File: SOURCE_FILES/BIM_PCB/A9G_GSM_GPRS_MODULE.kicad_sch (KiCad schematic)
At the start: 46 parts, among them J3 nano_sim, Q5 BSN20, U3 A9G_MODULE

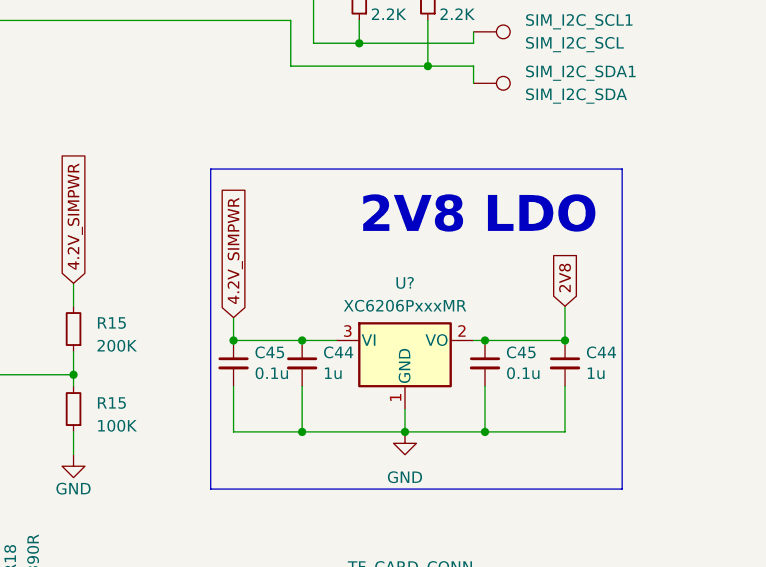
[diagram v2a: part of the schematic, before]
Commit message: completed gerber and placement
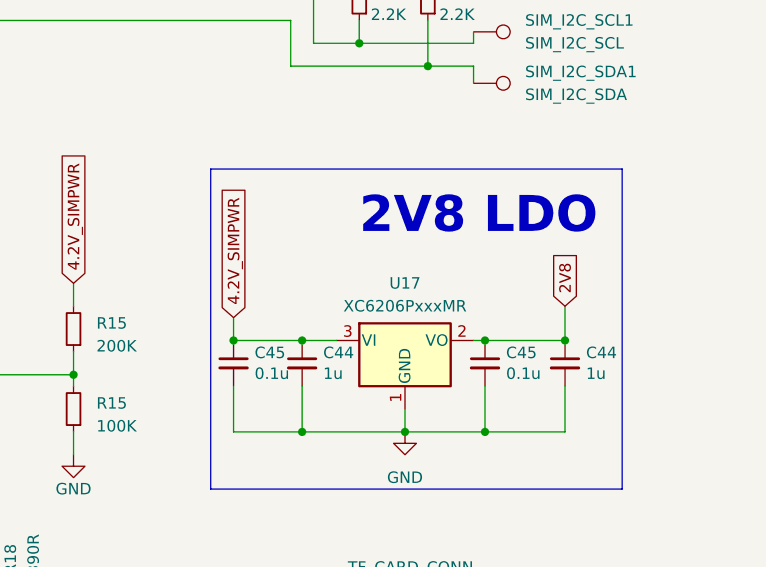
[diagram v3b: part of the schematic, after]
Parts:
- gave numbers to parts that had none: 1
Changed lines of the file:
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@@
           (reference "C15") (unit 1)
-        )
-        (path "/b79ebed7-e146-448b-8dab-0aefb3e182ca/2c1557a8-70b5-4535-b084-9e551cb55dcd/4ded7b71-30ec-4263-8ef5-be9822f9dd9f"
-          (reference "C?") (unit 1)
         )
       )
@@
           (reference "#PWR0125") (unit 1)
         )
-        (path "/b79ebed7-e146-448b-8dab-0aefb3e182ca/2c1557a8-70b5-4535-b084-9e551cb55dcd/4ded7b71-30ec-4263-8ef5-be9822f9dd9f"
-          (reference "#PWR0125") (unit 1)
-        )
       )
     )
@@
   (symbol (lib_id "Regulator_Linear:XC6206PxxxMR") (at 259.08 106.68 0) (unit 1)
     (in_bom yes) (on_board yes) (dnp no) (fields_autoplaced)
-    (property "Reference" "U?" (at 259.08 100.33 0)
+    (property "Reference" "U17" (at 259.08 100.33 0)
       (effects (font (size 1.27 1.27)))
     )
@@
     (instances
       (project "BIM_PCB"
-        (path "/b79ebed7-e146-448b-8dab-0aefb3e182ca/2c1557a8-70b5-4535-b084-9e551cb55dcd/4ded7b71-30ec-4263-8ef5-be9822f9dd9f"
-          (reference "U?") (unit 1)
-        )
         (path "/b79ebed7-e146-448b-8dab-0aefb3e182ca/2c1557a8-70b5-4535-b084-9e551cb55dcd"
           (reference "U17") (unit 1)
@@
           (reference "C16") (unit 1)
         )
-        (path "/b79ebed7-e146-448b-8dab-0aefb3e182ca/2c1557a8-70b5-4535-b084-9e551cb55dcd/4ded7b71-30ec-4263-8ef5-be9822f9dd9f"
-          (reference "C?") (unit 1)
-        )
       )
       (project "sd_card"
@@
           (reference "C14") (unit 1)
         )
-        (path "/b79ebed7-e146-448b-8dab-0aefb3e182ca/2c1557a8-70b5-4535-b084-9e551cb55dcd/4ded7b71-30ec-4263-8ef5-be9822f9dd9f"
-          (reference "C?") (unit 1)
-        )
       )
       (project "sd_card"
@@
           (reference "C17") (unit 1)
         )
-        (path "/b79ebed7-e146-448b-8dab-0aefb3e182ca/2c1557a8-70b5-4535-b084-9e551cb55dcd/4ded7b71-30ec-4263-8ef5-be9822f9dd9f"
-          (reference "C?") (unit 1)
-        )
-      )
+      )

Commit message: updates in BOM gerber and PCL
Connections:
- net GND: now also U3.29 (GND), U3.46 (GND); no longer U3.40 (GND)
- net GPS POSITION: now also U3.30 (IO28); no longer U3.39 (IO28)
- net Sim_CLK: now also U3.41 (SIM_CLK); no longer U3.28 (SIM_CLK)
- net Sim_DIO: now also U3.39 (SIM_DIO); no longer U3.30 (SIM_DIO)
- net V_Sim: now also U3.40 (VSIM); no longer U3.29 (VSIM)
- net at U3.31 (IO30): no longer D+1.1
- net at U3.32 (IO25): no longer D-1.1
- net at U3.33 (MIC_N): no longer D+1.1
- net at U3.34 (MIC_P): no longer D-1.1
- net at U3.35 (USB_N): now also D-1.1
- net at U3.36 (USB_P): now also D+1.1
- net at U3.37 (HST_TXD): now also D+1.1
- net at U3.38 (HST_RXD): now also D-1.1
- net at AE2.1 (A), D1.2 (A2), L2.2: now also U3.28 (GPS_RF); no longer U3.41 (GPS_RF)
- net i/o: now reaches D11.5 (K), J3.C7 (I/O), R15.2
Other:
- moved on the sheet: D+1, D-1, D13, R18
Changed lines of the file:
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@@
   (junction (at 108.585 91.44) (diameter 0) (color 0 0 0 0)
   )
-  (junction (at 157.48 170.18) (diameter 0) (color 0 0 0 0)
-  )
   (junction (at 73.025 91.44) (diameter 0) (color 0 0 0 0)
   )
@@
   (junction (at 247.65 106.68) (diameter 0) (color 0 0 0 0)
   )
+  (junction (at 165.1 170.18) (diameter 0) (color 0 0 0 0)
+  )
   (junction (at 267.97 106.68) (diameter 0) (color 0 0 0 0)
   )
@@
   (junction (at 62.865 29.21) (diameter 0) (color 0 0 0 0)
   )
+  (junction (at 170.18 170.18) (diameter 0) (color 0 0 0 0)
+  )
   (junction (at 247.65 116.84) (diameter 0) (color 0 0 0 0)
   )
   (no_connect (at 187.96 114.3))
   (no_connect (at 66.04 99.06))
-  (no_connect (at 134.62 152.4))
+  (no_connect (at 134.62 154.94))
   (no_connect (at 134.62 121.92))
   (no_connect (at 187.96 109.22))
@@
   (no_connect (at 187.96 111.76))
   (no_connect (at 187.96 91.44))
-  (no_connect (at 134.62 149.86))
+  (no_connect (at 134.62 152.4))
   (no_connect (at 134.62 134.62))
   (no_connect (at 187.96 93.98))
@@
     (stroke (width 0) (type default))
   )
+  (wire (pts (xy 165.1 165.1) (xy 165.1 170.18))
+    (stroke (width 0) (type default))
+  )
   (wire (pts (xy 187.96 142.24) (xy 252.73 142.24))
     (stroke (width 0) (type default))
@@
     (stroke (width 0) (type default))
   )
-  (wire (pts (xy 157.48 165.1) (xy 157.48 170.18))
-    (stroke (width 0) (type default))
-  )
-  (wire (pts (xy 157.48 170.18) (xy 162.56 170.18))
-    (stroke (width 0) (type default))
-  )
   (wire (pts (xy 240.03 116.84) (xy 247.65 116.84))
     (stroke (width 0) (type default))
@@
     (stroke (width 0) (type default))
   )
-  (wire (pts (xy 134.62 142.24) (xy 129.54 142.24))
+  (wire (pts (xy 134.62 144.78) (xy 128.905 144.78))
     (stroke (width 0) (type default))
   )
@@
     (stroke (width 0) (type default))
   )
+  (wire (pts (xy 170.18 165.1) (xy 170.18 170.18))
+    (stroke (width 0) (type default))
+  )
   (wire (pts (xy 109.22 40.64) (xy 134.62 40.64))
     (stroke (width 0) (type default))
@@
     (stroke (width 0) (type default))
   )
-  (wire (pts (xy 116.84 163.83) (xy 116.84 167.005))
+  (wire (pts (xy 116.84 166.37) (xy 116.84 169.545))
     (stroke (width 0) (type default))
   )
@@
     (stroke (width 0) (type default))
   )
+  (wire (pts (xy 170.18 170.18) (xy 172.72 170.18))
+    (stroke (width 0) (type default))
+  )
   (wire (pts (xy 100.33 93.98) (xy 134.62 93.98))
     (stroke (width 0) (type default))
@@
     (stroke (width 0) (type default))
   )
-  (wire (pts (xy 129.54 142.24) (xy 129.54 146.05))
+  (wire (pts (xy 128.905 144.78) (xy 128.905 148.59))
     (stroke (width 0) (type default))
   )
@@
     (stroke (width 0) (type default))
   )
-  (wire (pts (xy 116.84 154.94) (xy 134.62 154.94))
+  (wire (pts (xy 116.84 157.48) (xy 134.62 157.48))
     (stroke (width 0) (type default))
   )
@@
     (stroke (width 0) (type default))
   )
-  (wire (pts (xy 116.84 151.13) (xy 132.08 151.13))
+  (wire (pts (xy 116.84 153.67) (xy 132.08 153.67))
     (stroke (width 0) (type default))
   )
@@
     (stroke (width 0) (type default))
   )
-  (wire (pts (xy 152.4 170.18) (xy 157.48 170.18))
+  (wire (pts (xy 152.4 170.18) (xy 162.56 170.18))
     (stroke (width 0) (type default))
   )
@@
     (stroke (width 0) (type default))
   )
-  (wire (pts (xy 132.08 144.78) (xy 134.62 144.78))
+  (wire (pts (xy 132.08 147.32) (xy 134.62 147.32))
     (stroke (width 0) (type default))
   )
@@
     (stroke (width 0) (type default))
   )
-  (wire (pts (xy 129.54 146.05) (xy 116.84 146.05))
+  (wire (pts (xy 128.905 148.59) (xy 116.84 148.59))
     (stroke (width 0) (type default))
   )
@@
     (stroke (width 0) (type default))
   )
-  (wire (pts (xy 116.84 172.085) (xy 116.84 176.53))
+  (wire (pts (xy 116.84 174.625) (xy 116.84 179.07))
     (stroke (width 0) (type default))
   )
@@
     (stroke (width 0) (type default))
   )
+  (wire (pts (xy 165.1 170.18) (xy 170.18 170.18))
+    (stroke (width 0) (type default))
+  )
   (wire (pts (xy 269.24 24.765) (xy 269.24 24.13))
     (stroke (width 0) (type default))
@@
     (stroke (width 0) (type default))
   )
-  (wire (pts (xy 116.84 154.94) (xy 116.84 158.75))
+  (wire (pts (xy 116.84 157.48) (xy 116.84 161.29))
     (stroke (width 0) (type default))
   )
@@
     (stroke (width 0) (type default))
   )
-  (wire (pts (xy 162.56 170.18) (xy 172.72 170.18))
+  (wire (pts (xy 162.56 170.18) (xy 165.1 170.18))
     (stroke (width 0) (type default))
   )
-  (wire (pts (xy 132.08 151.13) (xy 132.08 144.78))
+  (wire (pts (xy 132.08 153.67) (xy 132.08 147.32))
     (stroke (width 0) (type default))
   )
@@
     (effects (font (size 1 1) bold) (justify right bottom))
   )
+  (label "i{slash}o" (at 69.85 101.6 0) (fields_autoplaced)
+    (effects (font (size 1.27 1.27)) (justify left bottom))
+  )
   (label "IO29" (at 97.79 59.69 0) (fields_autoplaced)
     (effects (font (size 1.27 1.27) bold) (justify left bottom))
@@
     (effects (font (size 1.27 1.27)) (justify right bottom))
   )
-  (label "GPS POSITION" (at 118.11 154.94 0) (fields_autoplaced)
+  (label "GPS POSITION" (at 118.11 157.48 0) (fields_autoplaced)
     (effects (font (size 1.27 1.27)) (justify left bottom))
   )
@@
     )
   )
-  (symbol (lib_id "Device:R_Small") (at 116.84 161.29 0) (mirror y) (unit 1)
+  (symbol (lib_id "Device:R_Small") (at 116.84 163.83 0) (mirror y) (unit 1)
     (in_bom yes) (on_board yes) (dnp no) (fields_autoplaced)
-    (property "Reference" "R18" (at 118.745 160.655 0)
+    (property "Reference" "R18" (at 118.745 163.195 0)
       (effects (font (size 1.27 1.27)) (justify right))
     )
-    (property "Value" "390R" (at 118.745 163.195 0)
+    (property "Value" "390R" (at 118.745 165.735 0)
       (effects (font (size 1.27 1.27)) (justify right))
     )
-    (property "Footprint" "Resistor_SMD:R_0402_1005Metric" (at 116.84 161.29 0)
+    (property "Footprint" "Resistor_SMD:R_0402_1005Metric" (at 116.84 163.83 0)
       (effects (font (size 1.27 1.27)) hide)
     )
-    (property "Datasheet" "~" (at 116.84 161.29 0)
+    (property "Datasheet" "~" (at 116.84 163.83 0)
       (effects (font (size 1.27 1.27)) hide)
     )
@@
     )
   )
-  (symbol (lib_id "Connector:TestPoint") (at 116.84 146.05 90) (mirror x) (unit 1)
+  (symbol (lib_id "Connector:TestPoint") (at 116.84 148.59 90) (mirror x) (unit 1)
     (in_bom yes) (on_board yes) (dnp no)
-    (property "Reference" "D+1" (at 111.125 144.78 90)
+    (property "Reference" "D+1" (at 111.125 147.32 90)
       (effects (font (size 1.27 1.27)) (justify left))
     )
-    (property "Value" "HST_RXD" (at 111.125 147.32 90)
+    (property "Value" "HST_RXD" (at 111.125 149.86 90)
       (effects (font (size 1.27 1.27)) (justify left))
     )
-    (property "Footprint" "brilliant-kicad-library:TestPoint_Pad_D0.9mm" (at 116.84 151.13 0)
+    (property "Footprint" "brilliant-kicad-library:TestPoint_Pad_D0.9mm" (at 116.84 153.67 0)
       (effects (font (size 1.27 1.27)) hide)
     )
-    (property "Datasheet" "~" (at 116.84 151.13 0)
+    (property "Datasheet" "~" (at 116.84 153.67 0)
       (effects (font (size 1.27 1.27)) hide)
     )
@@
     )
   )
-  (symbol (lib_id "Device:LED_Small") (at 116.84 169.545 90) (unit 1)
+  (symbol (lib_id "Device:LED_Small") (at 116.84 172.085 90) (unit 1)
     (in_bom yes) (on_board yes) (dnp no)
-    (property "Reference" "D13" (at 119.126 169.799 0)
+    (property "Reference" "D13" (at 119.126 172.339 0)
       (effects (font (size 1.27 1.27)))
     )
-    (property "Value" "BLUE" (at 118.745 169.4815 0)
+    (property "Value" "BLUE" (at 118.745 172.0215 0)
       (effects (font (size 1.27 1.27)) hide)
     )
-    (property "Footprint" "LED_SMD:LED_0603_1608Metric" (at 116.84 169.545 90)
+    (property "Footprint" "LED_SMD:LED_0603_1608Metric" (at 116.84 172.085 90)
       (effects (font (size 1.27 1.27)) hide)
     )
-    (property "Datasheet" "~" (at 116.84 169.545 90)
+    (property "Datasheet" "~" (at 116.84 172.085 90)
       (effects (font (size 1.27 1.27)) hide)
     )
@@
     )
   )
-  (symbol (lib_id "Connector:TestPoint") (at 116.84 151.13 90) (mirror x) (unit 1)
+  (symbol (lib_id "Connector:TestPoint") (at 116.84 153.67 90) (mirror x) (unit 1)
     (in_bom yes) (on_board yes) (dnp no)
-    (property "Reference" "D-1" (at 111.125 149.86 90)
+    (property "Reference" "D-1" (at 111.125 152.4 90)
       (effects (font (size 1.27 1.27)) (justify left))
     )
-    (property "Value" "HST_TXD" (at 111.125 152.4 90)
+    (property "Value" "HST_TXD" (at 111.125 154.94 90)
       (effects (font (size 1.27 1.27)) (justify left))
     )
-    (property "Footprint" "brilliant-kicad-library:TestPoint_Pad_D0.9mm" (at 116.84 156.21 0)
+    (property "Footprint" "brilliant-kicad-library:TestPoint_Pad_D0.9mm" (at 116.84 158.75 0)
       (effects (font (size 1.27 1.27)) hide)
     )
-    (property "Datasheet" "~" (at 116.84 156.21 0)
+    (property "Datasheet" "~" (at 116.84 158.75 0)
       (effects (font (size 1.27 1.27)) hide)
     )
@@
     )
   )
-  (symbol (lib_id "power:GND") (at 116.84 176.53 0) (unit 1)
+  (symbol (lib_id "power:GND") (at 116.84 179.07 0) (unit 1)
     (in_bom yes) (on_board yes) (dnp no) (fields_autoplaced)
-    (property "Reference" "#PWR0100" (at 116.84 182.88 0)
+    (property "Reference" "#PWR0100" (at 116.84 185.42 0)
       (effects (font (size 1.27 1.27)) hide)
     )
-    (property "Value" "GND" (at 116.84 181.61 0)
+    (property "Value" "GND" (at 116.84 184.15 0)
       (effects (font (size 1.27 1.27)))
     )
-    (property "Footprint" "" (at 116.84 176.53 0)
+    (property "Footprint" "" (at 116.84 179.07 0)
       (effects (font (size 1.27 1.27)) hide)
     )
-    (property "Datasheet" "" (at 116.84 176.53 0)
+    (property "Datasheet" "" (at 116.84 179.07 0)
       (effects (font (size 1.27 1.27)) hide)
     )

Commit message: completed project
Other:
- sheet TF_CARD_CONN ports: added 2V8; removed none
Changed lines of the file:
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@@
   (junction (at 257.81 64.135) (diameter 0) (color 0 0 0 0)
   )
-  (junction (at 67.31 55.88) (diameter 0) (color 0 0 0 0)
-  )
   (junction (at 203.2 40.64) (diameter 0) (color 0 0 0 0)
   )
@@
     (stroke (width 0) (type default))
   )
+  (wire (pts (xy 274.955 130.81) (xy 274.955 133.35))
+    (stroke (width 0) (type default))
+  )
   (wire (pts (xy 259.08 24.13) (xy 237.49 24.13))
     (stroke (width 0) (type default))
@@
     (stroke (width 0) (type default))
   )
-  (wire (pts (xy 79.375 55.88) (xy 67.31 55.88))
-    (stroke (width 0) (type default))
-  )
   (wire (pts (xy 31.75 170.18) (xy 30.48 170.18))
     (stroke (width 0) (type default))
@@
     )
   )
+  (global_label "2V8" (shape input) (at 274.955 130.81 90) (fields_autoplaced)
+    (effects (font (size 1.27 1.27)) (justify left))
+    (property "Intersheetrefs" "${INTERSHEET_REFS}" (at 274.955 124.3966 90)
+      (effects (font (size 1.27 1.27)) (justify left) hide)
+    )
+  )
   (global_label "2V8" (shape input) (at 276.86 102.87 90) (fields_autoplaced)
     (effects (font (size 1.27 1.27)) (justify left))
@@
       (effects (font (size 1.27 1.27)) (justify left))
     )
+    (pin "2V8" input (at 274.955 133.35 90)
+      (effects (font (size 1.27 1.27)) (justify right))
+    )
     (instances

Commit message: completed project and all the prouction files
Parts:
- removed C2 (x3): 22p, Capacitor_SMD:C_0402_1005Metric, symbol Device:C_Small
- removed C26 (x2): 1u, Capacitor_SMD:C_0402_1005Metric, symbol Device:C_Small
- removed C29: 100u, Capacitor_Tantalum_SMD:CP_EIA-3216-18_Kemet-A, symbol Device:C_Polarized
- removed C44 (x2): 1u, Capacitor_SMD:C_0402_1005Metric, symbol fridgeduino-rescue:C_Small-Device
- removed C45 (x2): 0.1u, Capacitor_SMD:C_0402_1005Metric, symbol fridgeduino-rescue:C_Small-Device
- removed D+1: HST_RXD, brilliant-kicad-library:TestPoint_Pad_D0.9mm, symbol Connector:TestPoint
- removed D+1: D+, brilliant-kicad-library:TestPoint_Pad_D0.9mm, symbol Connector:TestPoint
- removed D-1: D-, brilliant-kicad-library:TestPoint_Pad_D0.9mm, symbol Connector:TestPoint
- removed D-1: HST_TXD, brilliant-kicad-library:TestPoint_Pad_D0.9mm, symbol Connector:TestPoint
- removed L2: 82nH, Inductor_SMD:L_0402_1005Metric, symbol Device:L
- removed Q5 (x2): BSN20, Package_TO_SOT_SMD:SOT-23, symbol Transistor_FET:BSN20
- removed R15: 200K, Resistor_SMD:R_0402_1005Metric, symbol Device:R_Small
- removed R15 (x3): 22R, Resistor_SMD:R_0402_1005Metric, symbol Device:R_Small
- removed R15 (x3): 1k, Resistor_SMD:R_0402_1005Metric, symbol Device:R_Small
- removed R15 (x3): 10K, Resistor_SMD:R_0402_1005Metric, symbol Device:R_Small
- removed R15: 100K, Resistor_SMD:R_0402_1005Metric, symbol Device:R_Small
- removed R16 (x2): 2.2K, Resistor_SMD:R_0402_1005Metric, symbol Device:R_Small
- removed R18 (x2): 390R, Resistor_SMD:R_0402_1005Metric, symbol Device:R_Small
- removed SIM_I2C_SCL1: SIM_I2C_SCL, brilliant-kicad-library:TestPoint_Pad_D0.9mm, symbol Connector:TestPoint
- removed SIM_I2C_SDA1: SIM_I2C_SDA, brilliant-kicad-library:TestPoint_Pad_D0.9mm, symbol Connector:TestPoint
- removed U17: XC6206PxxxMR, Package_TO_SOT_SMD:SOT-23-3, symbol Regulator_Linear:XC6206PxxxMR
- added AE3: Antenna_Shield, greencharge-footprints:UFL_COAX_CONN23370191, symbol Device:Antenna_Shield
- added C19, C45 (x2): 0.1u, Capacitor_SMD:C_0402_1005Metric, symbol fridgeduino-rescue:C_Small-Device
- added C2 (x3): 22p, Capacitor_SMD:C_0402_1005Metric, symbol Device:C_Small
- added C26 (x2): 1u, Capacitor_SMD:C_0402_1005Metric, symbol Device:C_Small
- added C36, C39: 100u, Capacitor_Tantalum_SMD:CP_EIA-3216-18_Kemet-A, symbol Device:C_Polarized
- added C44 (x2): 1u, Capacitor_SMD:C_0402_1005Metric, symbol fridgeduino-rescue:C_Small-Device
- added D+1: HST_RXD, brilliant-kicad-library:TestPoint_Pad_D0.9mm, symbol Connector:TestPoint
- added D+1: D+, brilliant-kicad-library:TestPoint_Pad_D0.9mm, symbol Connector:TestPoint
- added D-1: HST_TXD, brilliant-kicad-library:TestPoint_Pad_D0.9mm, symbol Connector:TestPoint
- added D-1: D-, brilliant-kicad-library:TestPoint_Pad_D0.9mm, symbol Connector:TestPoint
- added FL1: SAFEB1G57KE0F00R15, Filter:Filter_1411-5_1.4x1.1mm, symbol Filter:SF14-1575F5UUC1
- added L3: 82nH, Inductor_SMD:L_0402_1005Metric, symbol Device:L
- added Q5 (x2): IRLML0100TRPBF, Package_TO_SOT_SMD:SOT-23, symbol Transistor_FET:BSN20
- added R15 (x3): 1k, Resistor_SMD:R_0402_1005Metric, symbol Device:R_Small
- added R15 (x3): 10K, Resistor_SMD:R_0402_1005Metric, symbol Device:R_Small
- added R15: 200K, Resistor_SMD:R_0402_1005Metric, symbol Device:R_Small
- added R15 (x3): 22R, Resistor_SMD:R_0402_1005Metric, symbol Device:R_Small
- added R15: 100K, Resistor_SMD:R_0402_1005Metric, symbol Device:R_Small
- added R16 (x2): 2.2K, Resistor_SMD:R_0402_1005Metric, symbol Device:R_Small
- added R18 (x2): 390R, Resistor_SMD:R_0402_1005Metric, symbol Device:R_Small
- added R51: 0R, Resistor_SMD:R_0402_1005Metric, symbol Device:R_US
- added U5: XC6206PxxxMR, Package_TO_SOT_SMD:SOT-23-3, symbol Regulator_Linear:XC6206PxxxMR
- AE2: footprint greencharge-footprints:UFL_COAX_CONN23370191 -> Connector_Coaxial:SMA_Samtec_SMA-J-P-X-ST-EM1_EdgeMount; MPN (none) -> SMA-KE-347-H13.5-1.2
- D12, D13: footprint LED_SMD:LED_0603_1608Metric -> LED_SMD:LED_0402_1005Metric
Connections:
- net MOSFET_LOGIC_LEVEL_TRANSLATOR6/LOW_SIDE_LOGIC_SIGNAL is gone; now on net GPS_TXD: U3.50 (UART2_TXD/IO5)
- net MOSFET_LOGIC_LEVEL_TRANSLATOR7/LOW_SIDE_LOGIC_SIGNAL is gone; now on net GPS_RXD: U3.49 (UART2_RXD/IO4)
- net MOSFET_LOGIC_LEVEL_TRANSLATOR8/LOW_SIDE_LOGIC_SIGNAL is gone; now on net Sim_Rx: U3.53 (UART1_RXD/IO0)
- net MOSFET_LOGIC_LEVEL_TRANSLATOR9/LOW_SIDE_LOGIC_SIGNAL is gone; now on net Sim_Tx: U3.54 (UART1_TXD/IO1)
- net 2V8: now also C44.1, C45.1, U5.2 (VO)
- net 4.2V_SIMPWR: now also C26.1, C36.1, C39.1, C44.1, C45.1, L3.2, R15.2, U5.3 (VI)
- net GND: now also AE3.2 (Shield), C19.1, C2.2, C2.2, C2.2, C26.2, C26.2, C36.2, C39.2, C44.2, C44.2, C45.2, C45.2, FL1.2, FL1.3, FL1.5, Q5.2 (S), Q5.2 (S), R15.1, R15.1, R15.1, U5.1 (GND)
- net GPRS_NET-STATUS: now also R18.1
- net GPS POSITION: now also R18.1
- net IO29: now also R15.1
- net PWRKEY: now also R15.1
- net Sim_CLK: now also C2.1, R15.1
- net Sim_DIO: now also C2.1, R15.1
- net Sim_RST: now also C2.1, R15.1
- net Sim_Restart: now also R15.1
- net VIO: now also C26.1, R15.2, R16.2, R16.2
- net V_Sim: now also C19.2
- net at U3.15 (ADC0): now also R15.1, R15.2
- net at D11.4 (K), J3.C3 (CLK): now also R15.2
- net at U3.1 (I2C2_SCL/IO19): now also R16.1
- net at U3.18 (RESET): now also Q5.3 (D)
- net at U3.2 (I2C2_SDA/IO20): now also R16.1
- net at U3.35 (USB_N): now also D-1.1
- net at U3.36 (USB_P): now also D+1.1
- net at U3.37 (HST_TXD): now also D+1.1
- net at U3.38 (HST_RXD): now also D-1.1
- net at U3.45 (GSM_RF): now also R51.1; no longer AE1.1 (A)
- net at U3.9 (PWR_KEY): now also Q5.3 (D), R15.1, R15.2
- net at D13.2 (A): now also R18.2
- net at D11.3 (K), J3.C2 (RST): now also R15.2
- net at D12.2 (A): now also R18.2
- net i/o: no longer names the net of D11.5 (K), J3.C7 (I/O)
- net i/o: now also R15.2
- new net: AE2.1 (A), AE3.1 (A), FL1.1, L3.1
- new net: Q5.1 (G), R15.2, R15.2 (x2)
- new net: FL1.4, U3.28 (GPS_RF)
- new net: AE1.1 (A), D1.2 (A2), R51.2
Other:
- removed sheet MOSFET_LOGIC_LEVEL_TRANSLATOR6
- removed sheet MOSFET_LOGIC_LEVEL_TRANSLATOR7
- removed sheet MOSFET_LOGIC_LEVEL_TRANSLATOR8
- removed sheet MOSFET_LOGIC_LEVEL_TRANSLATOR9

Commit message: all items updated
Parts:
- removed AE3: Antenna_Shield, greencharge-footprints:UFL_COAX_CONN23370191, symbol Device:Antenna_Shield
- added C21, C22: C_Small, Capacitor_SMD:C_0402_1005Metric, symbol Device:C_Small
- added R17: 22R, Resistor_SMD:R_0402_1005Metric, symbol Device:R_US
- AE2: footprint Connector_Coaxial:SMA_Samtec_SMA-J-P-X-ST-EM1_EdgeMount -> Connector_Coaxial:SMA_Molex_73251-2200_Horizontal; MPN SMA-KE-347-H13.5-1.2 -> BWSMA-KWE-Z001
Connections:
- net GND: now also C21.1, C22.1
- net GPS_RXD: now also U3.50 (UART2_RXD/IO5); no longer U3.49 (UART2_RXD/IO4)
- net GPS_TXD: now also U3.49 (UART2_TXD/IO4); no longer U3.50 (UART2_TXD/IO5)
- net at AE2.1 (A), FL1.1: now also R17.2; no longer L3.1
- net at R51.1, U3.45 (GSM_RF): now also C21.2
- net at AE1.1 (A), D1.2 (A2), R51.2: now also C22.2
- new net: L3.1, R17.1
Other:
- moved on the sheet: L3, R16
